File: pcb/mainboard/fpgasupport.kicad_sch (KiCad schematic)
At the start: 30 parts, among them J5 XILINX_JTAG, M1 960-23-23-F-AB-0, U8 XC7K70T-2FBG484C

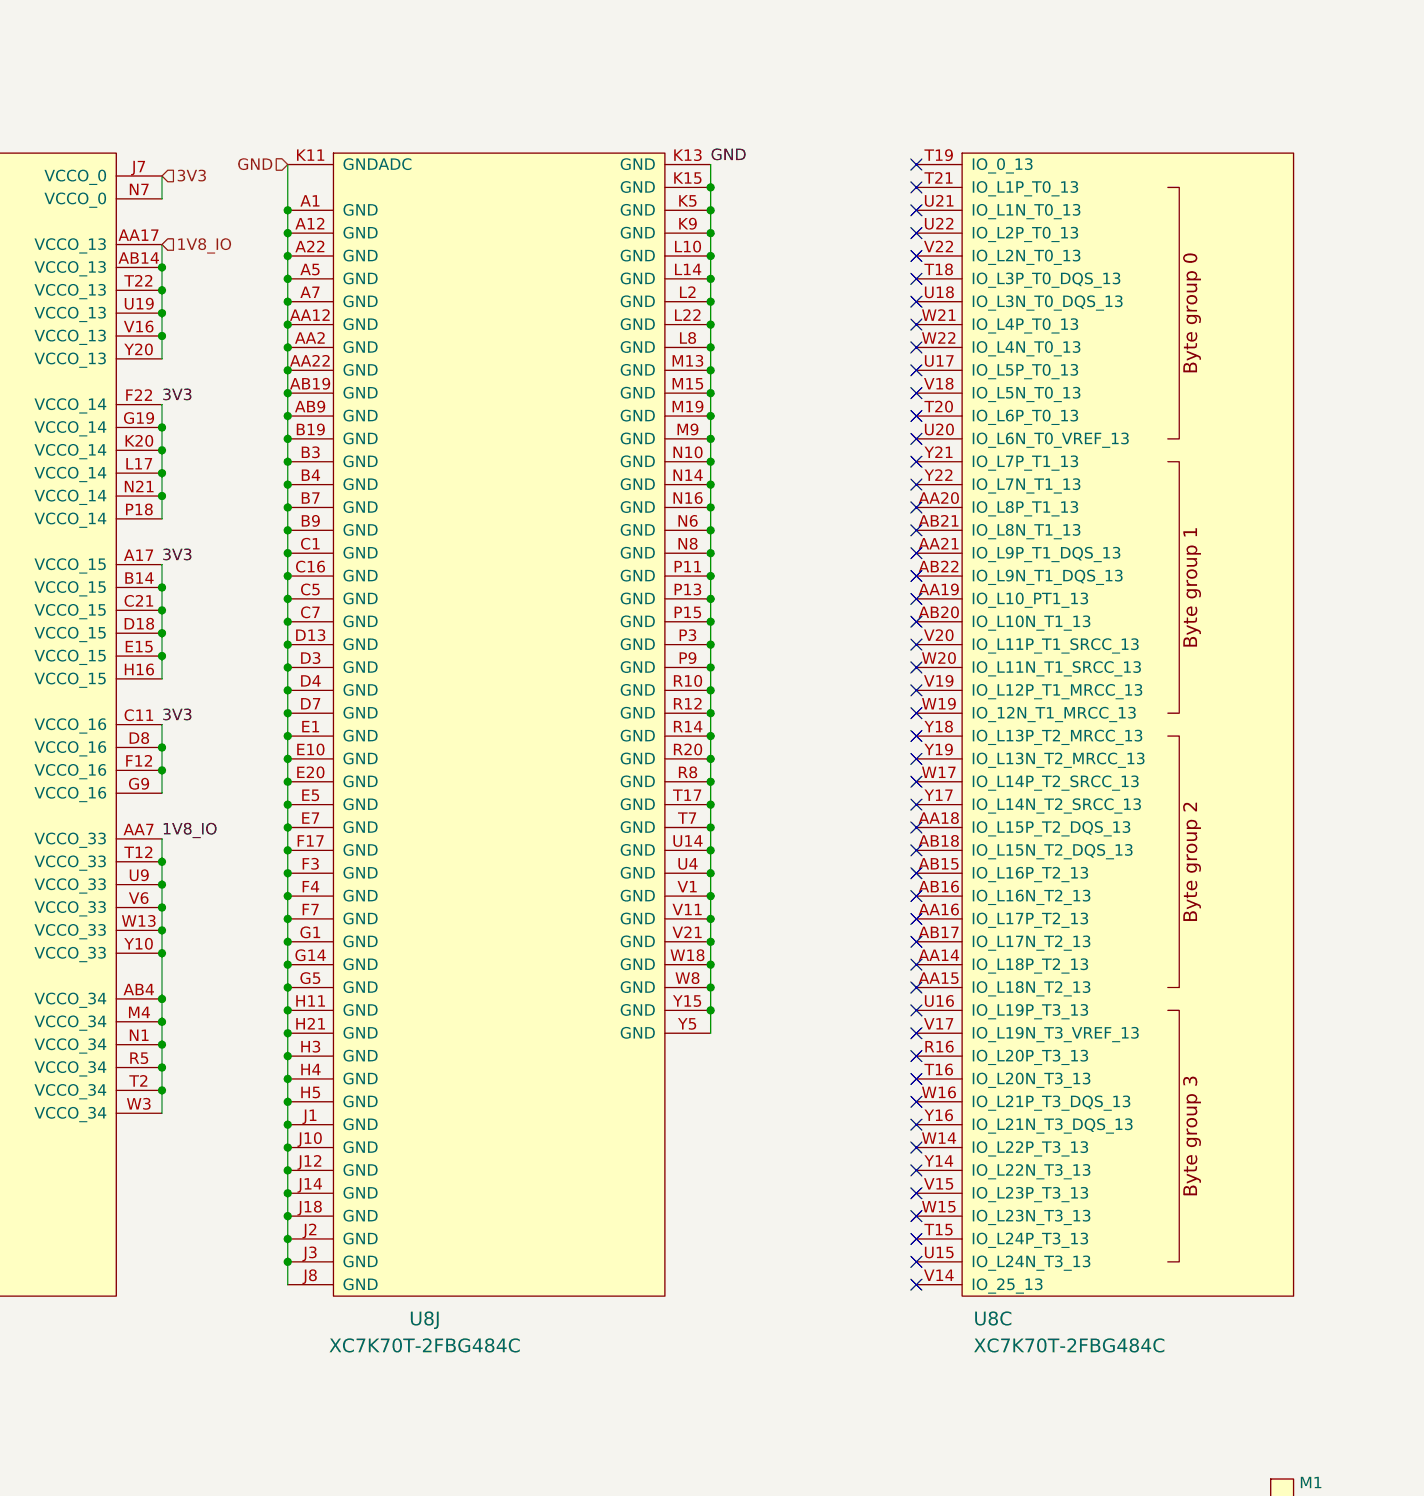
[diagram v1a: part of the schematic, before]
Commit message: Initial FPGA routing
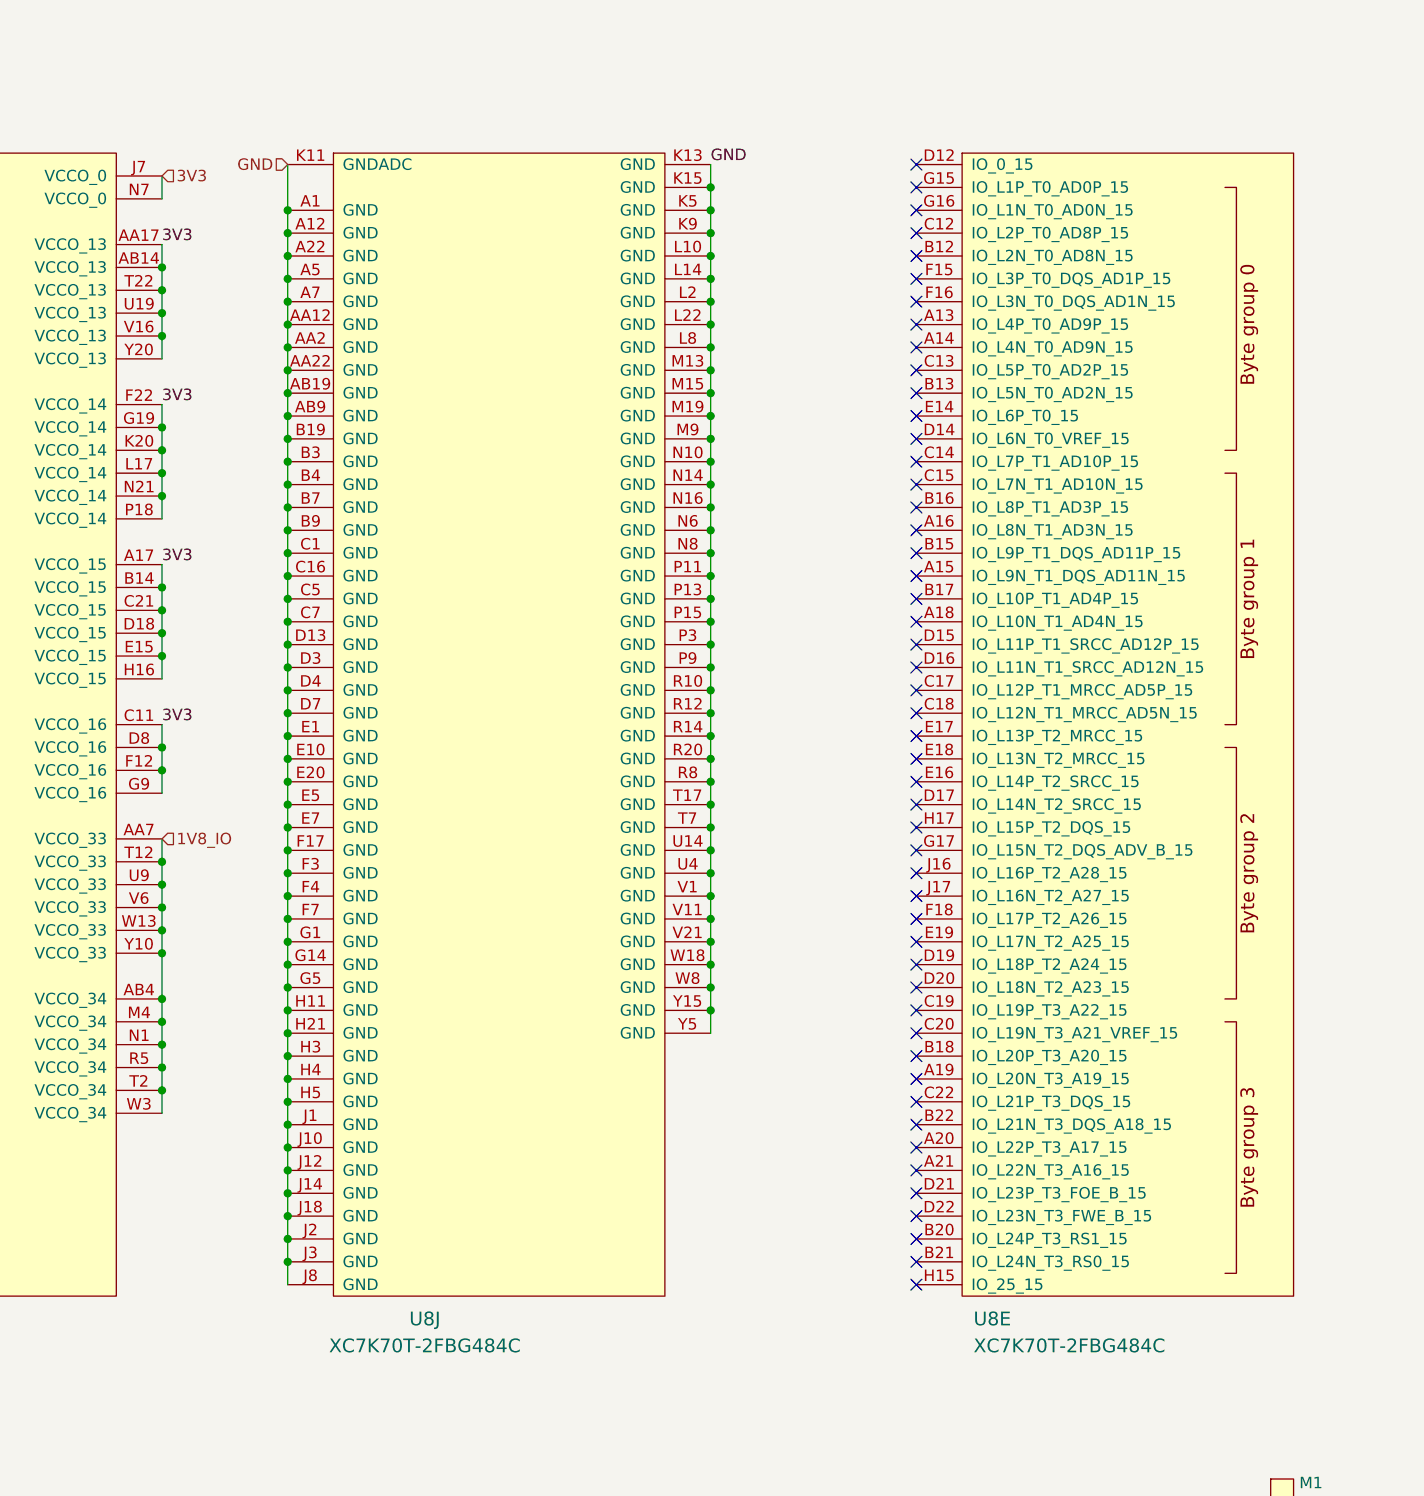
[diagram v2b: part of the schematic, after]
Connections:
- net 1V8_IO: no longer U8.AA17 (VCCO_13), U8.AB14 (VCCO_13), U8.T22 (VCCO_13), U8.U19 (VCCO_13), U8.V16 (VCCO_13), U8.Y20 (VCCO_13)
- net 3V3: now also U8.AA17 (VCCO_13), U8.AB14 (VCCO_13), U8.T22 (VCCO_13), U8.U19 (VCCO_13), U8.V16 (VCCO_13), U8.Y20 (VCCO_13)
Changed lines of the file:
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@@
   (title_block
     (title "Trigger Crossbar")
-    (date "2023-12-20")
+    (date "2023-12-22")
     (rev "0.1")
     (company "Antikernel Labs")
@@
     (effects (font (size 1.27 1.27)) (justify right bottom))
   )
+  (label "3V3" (at 175.26 50.8 0)
+    (effects (font (size 1.27 1.27)) (justify left bottom))
+  )
   (label "FPGA_JTAG_TCK" (at 77.47 130.81 180)
     (effects (font (size 1.27 1.27)) (justify right bottom))
@@
     (effects (font (size 1.27 1.27)) (justify right bottom))
   )
-  (label "1V8_IO" (at 175.26 116.84 0)
-    (effects (font (size 1.27 1.27)) (justify left bottom))
-  )
   (label "GND" (at 35.56 35.56 180)
     (effects (font (size 1.27 1.27)) (justify right bottom))
@@
     (effects (font (size 1.27 1.27)) (justify right))
   )
-  (hierarchical_label "1V8_IO" (shape input) (at 175.26 50.8 0)
+  (hierarchical_label "1V8_IO" (shape input) (at 175.26 116.84 0)
     (effects (font (size 1.27 1.27)) (justify left))
   )
@@
     (pin "2")
   )
-  (symbol (lib_id "xilinx-azonenberg:XC7KxT-FBG484") (at 264.16 166.37 0) (unit 3)
+  (symbol (lib_id "xilinx-azonenberg:XC7KxT-FBG484") (at 264.16 166.37 0) (unit 5)
     (in_bom yes) (on_board yes)
     (property "Reference" "U8" (id 0) (at 265.43 170.18 0)

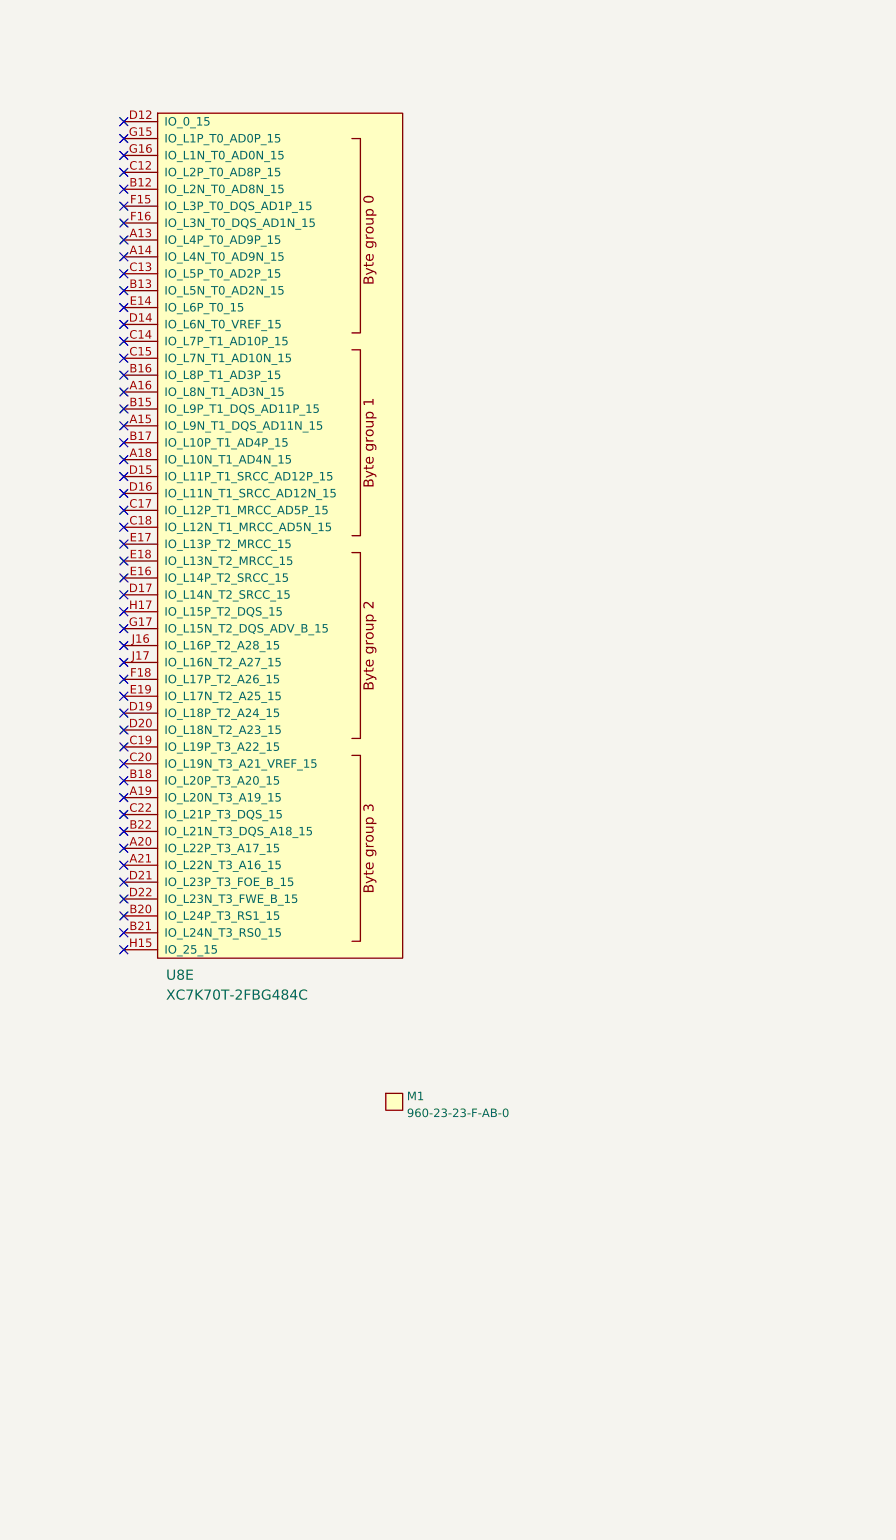
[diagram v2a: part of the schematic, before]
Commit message: Hooked up most input pins
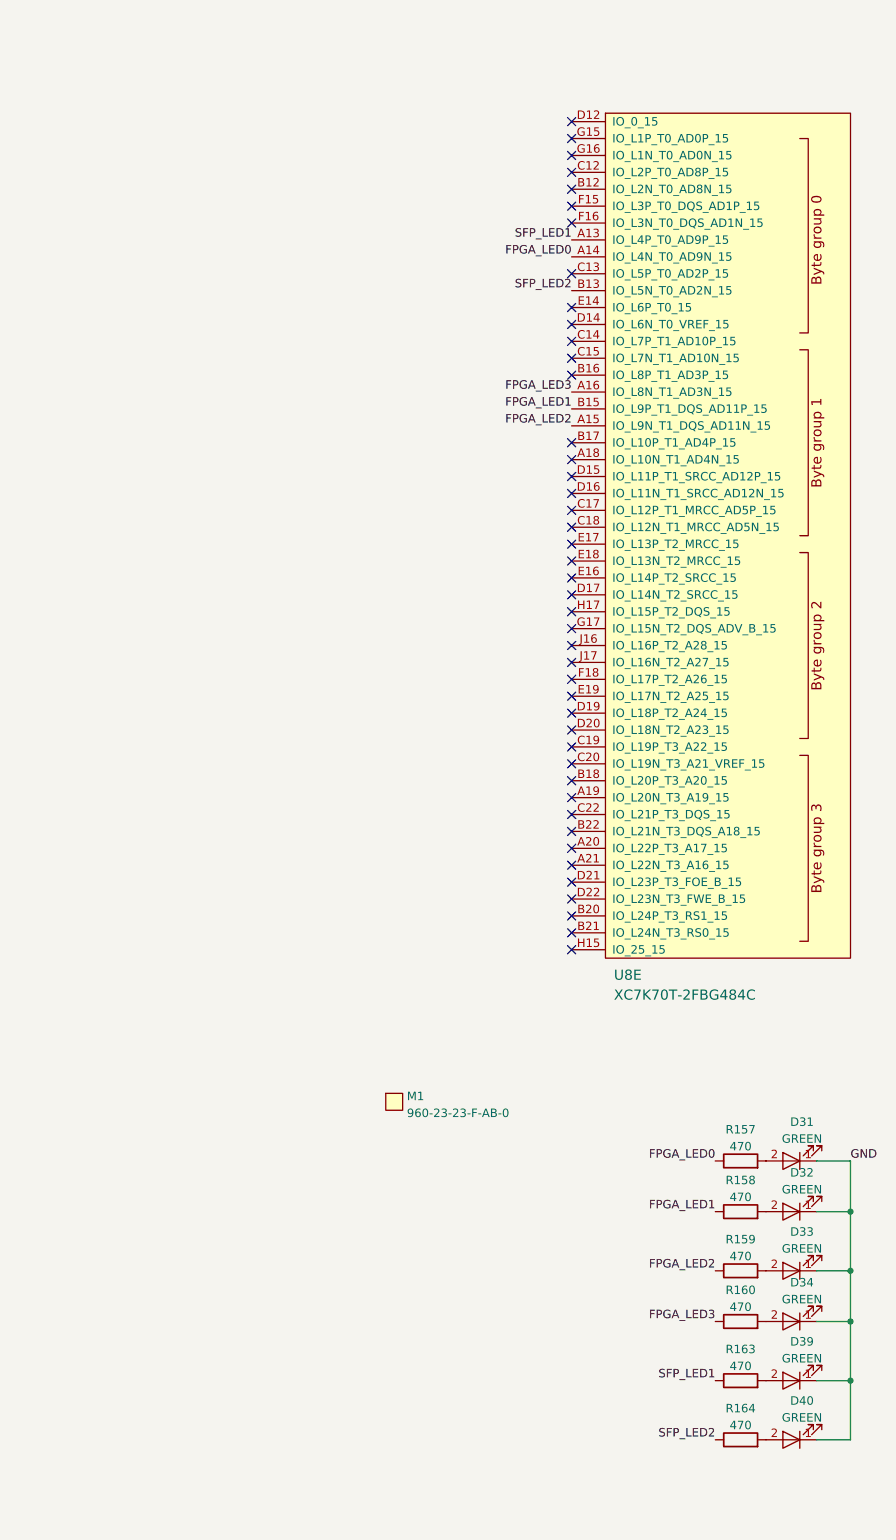
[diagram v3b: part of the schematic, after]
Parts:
- added D31, D32, D33, D34, D39, D40: GREEN, azonenberg_pcb:EIA_0603_LED, symbol device:LED
- added R157, R158, R159, R160, R163, R164: 470, azonenberg_pcb:EIA_0402_RES_NOSILK, symbol device:R
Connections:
- net GND: now also D31.1 (K), D32.1 (K), D33.1 (K), D34.1 (K), D39.1 (K), D40.1 (K)
- net SFP_LED1: now reaches U8.A13 (IO_L4P_T0_AD9P_15)
- net SFP_LED1: now also R163.1
- net FPGA_LED0: now reaches U8.A14 (IO_L4N_T0_AD9N_15)
- net FPGA_LED0: now also R157.1
- net FPGA_LED2: now reaches U8.A15 (IO_L9N_T1_DQS_AD11N_15)
- net FPGA_LED2: now also R159.1
- net FPGA_LED3: now reaches U8.A16 (IO_L8N_T1_AD3N_15)
- net FPGA_LED3: now also R160.1
- net SFP_LED2: now reaches U8.B13 (IO_L5N_T0_AD2N_15)
- net SFP_LED2: now also R164.1
- net FPGA_LED1: now reaches U8.B15 (IO_L9P_T1_DQS_AD11P_15)
- net FPGA_LED1: now also R158.1
- new net: D32.2 (A), R158.2
- new net: D34.2 (A), R160.2
- new net: D31.2 (A), R157.2
- new net: D39.2 (A), R163.2
- new net: D33.2 (A), R159.2
- new net: D40.2 (A), R164.2
- no-connect marks 52 -> 46
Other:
- moved on the sheet: U8E
